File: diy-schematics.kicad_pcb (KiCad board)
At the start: 2 copper layers, 85 x 39 mm, 25 parts, among them J2 GAINCON, J3 AUDIO_JACK, J4 USB_SOK, J5 USB_CON, J6 MIC_CON1, U1 THAT1512PO8-U1, U2 NMA0515SC

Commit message: fixes to new PCB
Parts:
- J3: value AUDIO_JACK -> Conn_01x02_Female; footprint Connector_JST:JST_XH_B3B-XH-A_1x03_P2.50mm_Vertical -> Connector_JST:JST_XH_B2B-XH-A_1x02_P2.50mm_Vertical
- moved J3 0.51 mm to (68.8, 177.0)
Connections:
- J3 pad 2: Net-(C8-Pad2) -> Earth
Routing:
- net Earth: track 346.4 -> 3.78 mm
- net Net-(C8-Pad2): track 10.0 -> 7.27 mm
- added copper zone on F.Cu, net Earth
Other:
- board text added: "1"
- board text added: "2"
- board text added: "3"
- board text added: "D+"
- board text added: "D-"
- board text added: "MIC+"
- board text added: "MIC-"
- board text added: "USB+5V"
- board text added: "USB_GND"

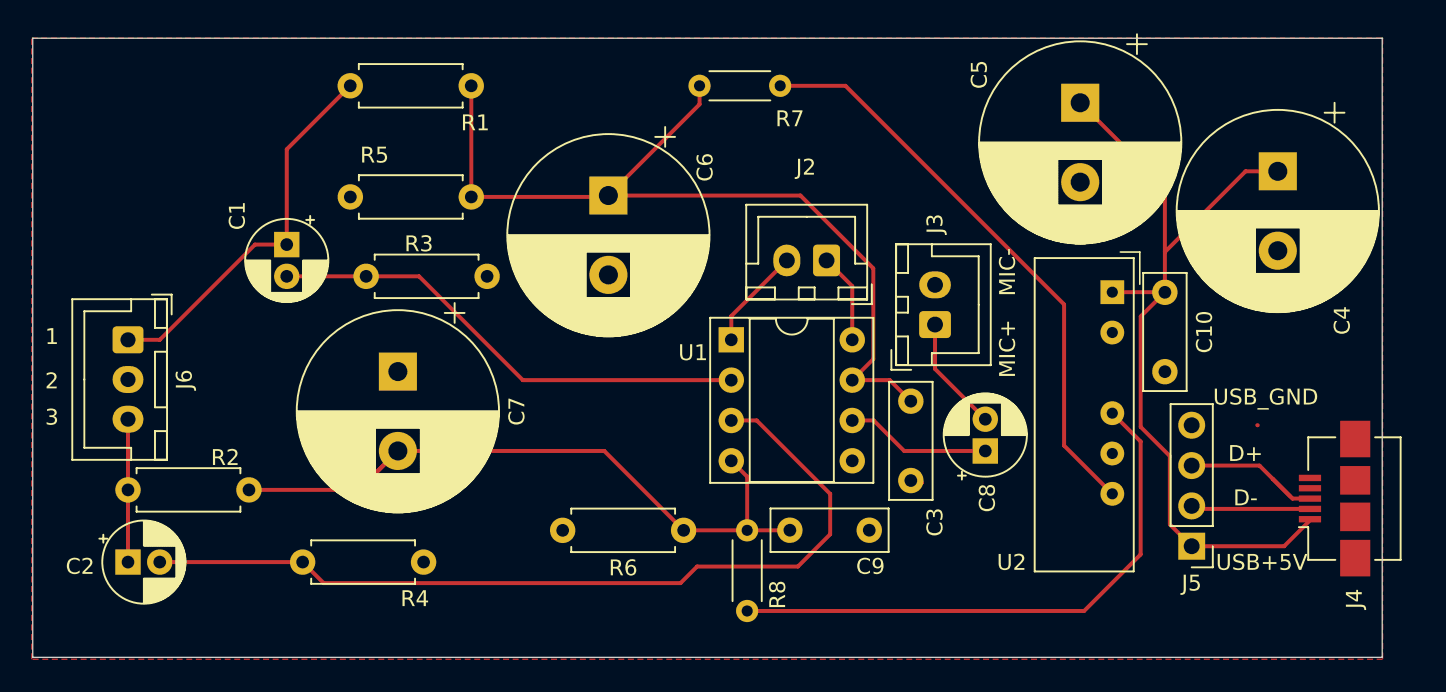
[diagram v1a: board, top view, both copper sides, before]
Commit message: reduce footprint of PCB
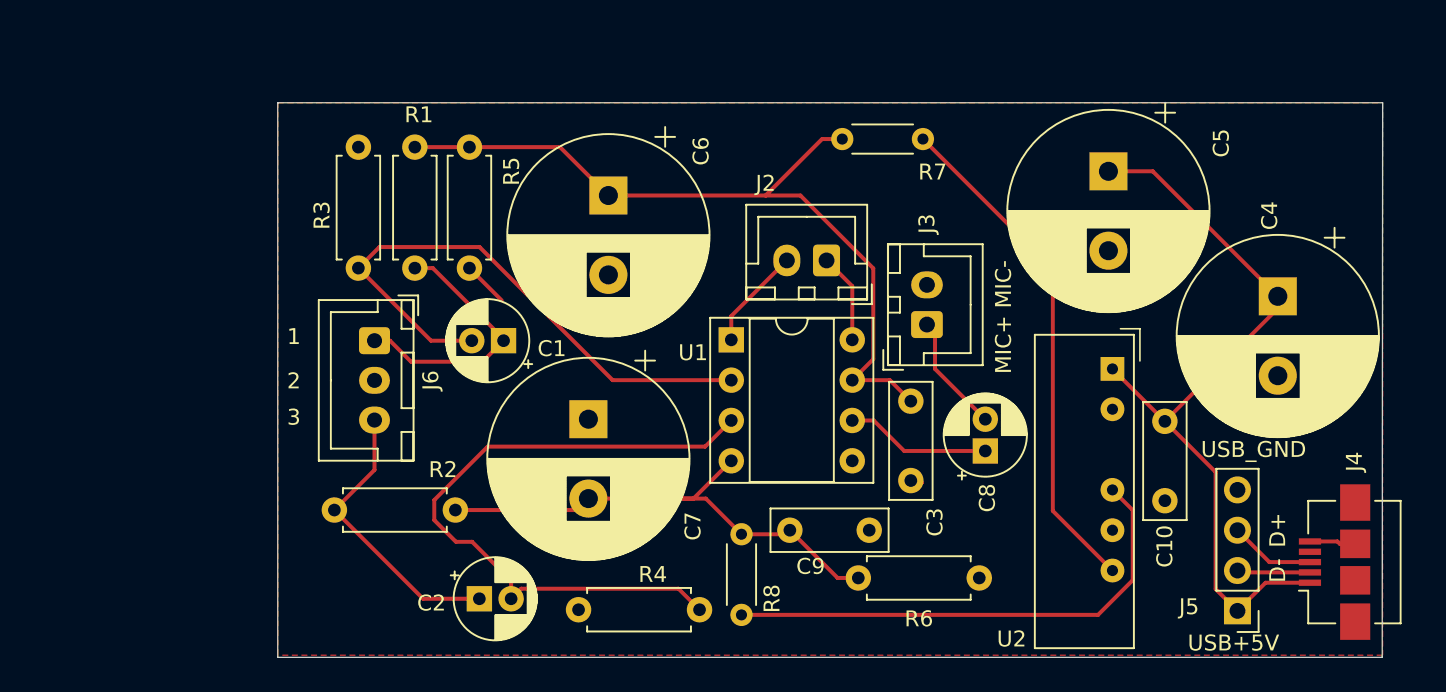
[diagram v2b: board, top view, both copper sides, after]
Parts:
- moved R4 25.2 mm to (54.0, 195.0), turned to 180 degrees
- moved C2 22.3 mm to (40.1, 194.3)
- moved J6 15.5 mm to (33.5, 178.1)
- moved C1 14.9 mm to (41.7, 178.1), turned to 180 degrees
- moved R2 13.1 mm to (31.0, 188.7)
- moved C7 12.4 mm to (47.0, 183.0)
- moved R1 12.2 mm to (36.1, 173.5), turned to 90 degrees
- moved R6 11.4 mm to (64.0, 193.0), turned to 0 degrees
- moved R7 9.60 mm to (63.0, 165.4)
- moved C10 8.13 mm to (83.3, 183.1)
- moved C4 7.87 mm to (90.4, 175.3)
- moved J5 4.99 mm to (87.9, 195.1)
- moved U2 4.83 mm to (80.0, 179.8)
- moved C5 4.67 mm to (79.8, 167.4)
- moved J4 4.00 mm to (94.0, 192.0)
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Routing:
- net Net-(C7-Pad2): track 44.8 -> 32.1 mm
- net Net-(C2-Pad2): track 54.7 -> 42.3 mm
- net Net-(C2-Pad1): track 9.00 -> 18.2 mm
- net Net-(C1-Pad1): track 24.1 -> 16.8 mm
- net Net-(C1-Pad2): track 30.7 -> 36.5 mm
- net Net-(C3-Pad1): track 55.4 -> 50.3 mm
- net +15V: track 36.8 -> 32.1 mm
- net Net-(J4-Pad3): track 9.90 -> 5.40 mm
- net VBUS: track 52.8 -> 48.6 mm
- net Earth: track 3.78 -> 7.93 mm
- net -15V: track 35.9 -> 31.8 mm
- net Net-(J4-Pad2): track 7.62 -> 4.98 mm
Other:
- board size 85 x 39 mm -> 69.6 x 34.9 mm

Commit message: added mounting holes, rendered gerber files
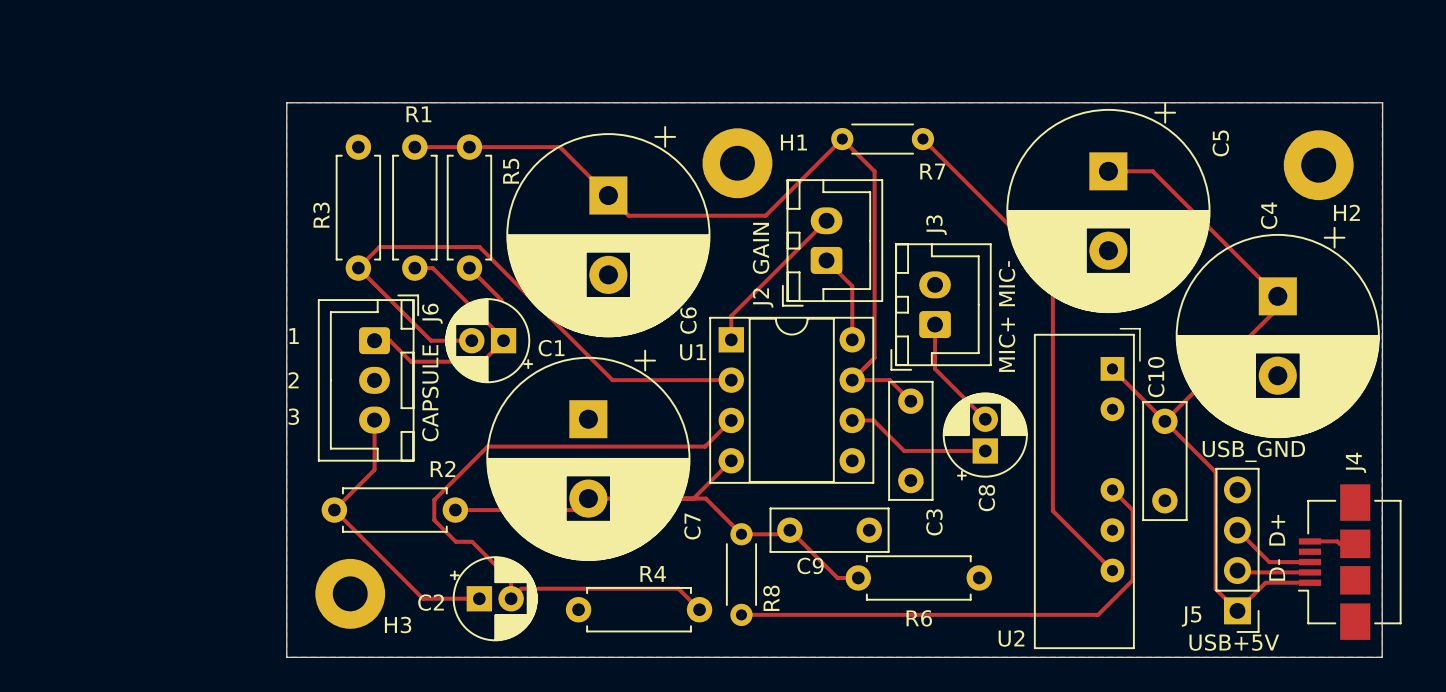
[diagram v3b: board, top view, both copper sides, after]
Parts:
- added H1: MountingHole_Pad, MountingHole:MountingHole_2.2mm_M2_Pad, F.Cu at (56.4, 166.9)
- added H2: MountingHole_Pad, MountingHole:MountingHole_2.2mm_M2_Pad, F.Cu at (93.0, 167.0)
- added H3: MountingHole_Pad, MountingHole:MountingHole_2.2mm_M2_Pad, F.Cu at (32.0, 194.0)
- moved J3 0.51 mm to (68.8, 177.0)
- turned J2 to 90 degrees
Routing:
- net Net-(C3-Pad1): track 50.3 -> 55.0 mm
- net Net-(J2-Pad2): track 6.45 -> 9.99 mm
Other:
- board size 69.6 x 34.9 mm -> 69 x 34.9 mm
- board text added: "CAPSULE"
- board text added: "GAIN"

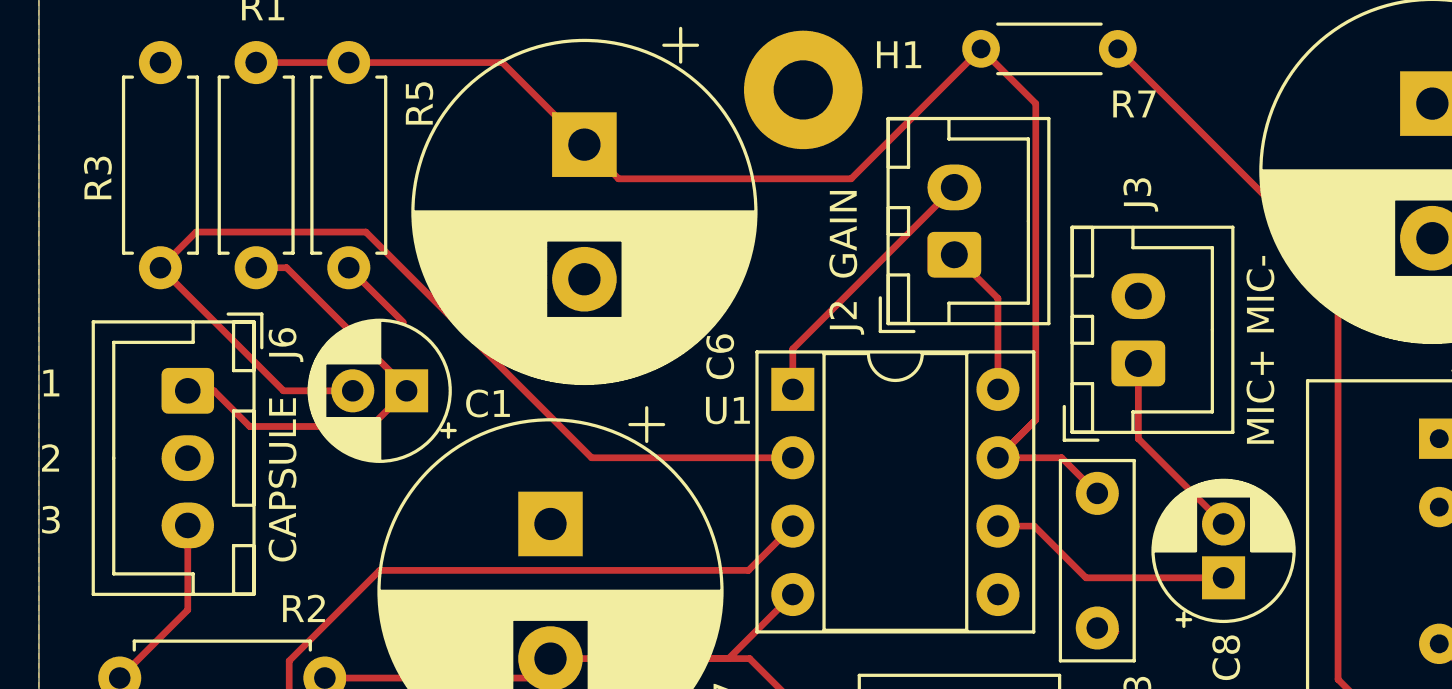
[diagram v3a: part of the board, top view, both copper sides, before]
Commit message: swap MIC+ and MIC-
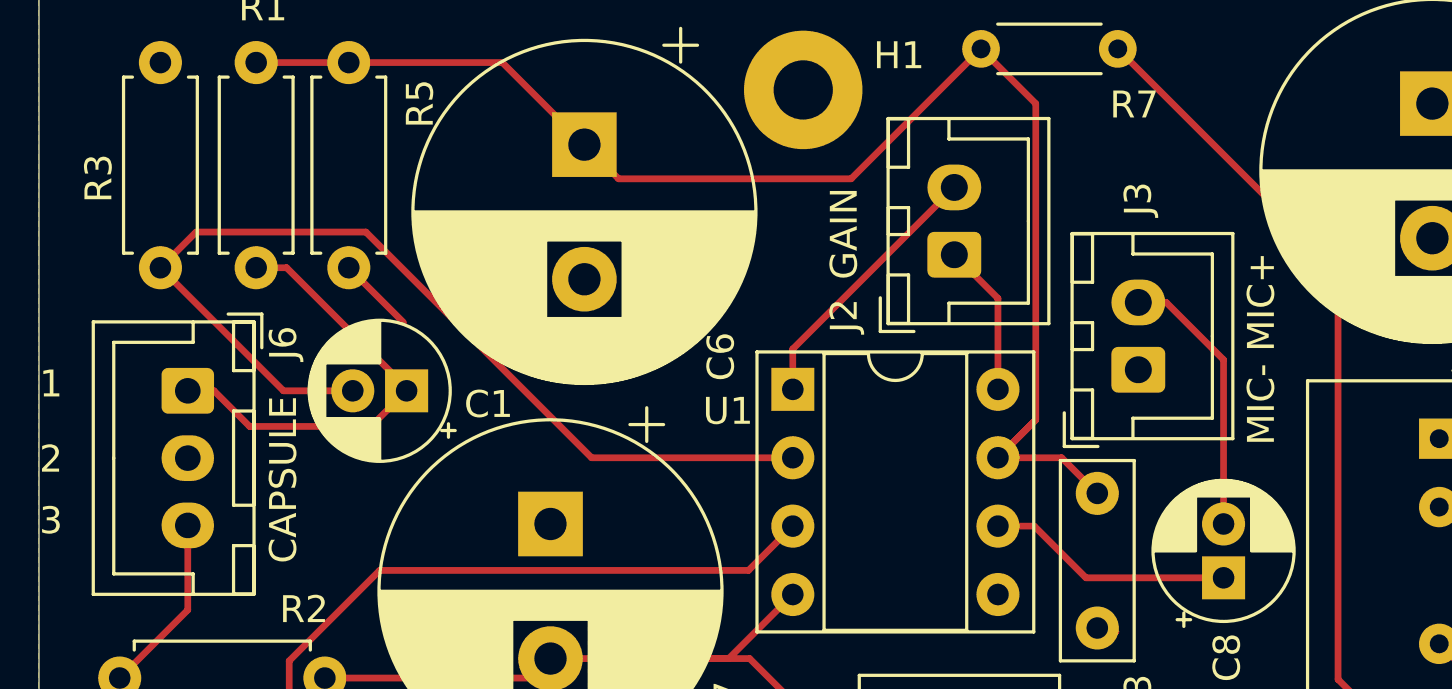
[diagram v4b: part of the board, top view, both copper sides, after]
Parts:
- moved J3 0.23 mm to (68.8, 177.3)
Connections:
- J3 pad 1: Net-(C8-Pad2) -> Earth
- J3 pad 2: Earth -> Net-(C8-Pad2)
- J4 pad 4: Net-(J4-Pad4) -> unconnected-(J4-Pad4)
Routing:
- net Net-(C8-Pad2): track 7.27 -> 10.1 mm
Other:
- net class Default removed
